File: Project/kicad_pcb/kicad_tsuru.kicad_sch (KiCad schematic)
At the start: 71 parts, among them J1 USB_C_Receptacle_USB2.0, J2 Conn_ARM_SWD_TagConnect_TC203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, J3 Conn_01x05_Pin, SW1 RotaryEncoder_Switch, U2 AP2112K-3.3, U3 STM32F072C8Tx

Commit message: cap & HS collision fixed
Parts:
- SW?: footprint PCM_marbastlib-various:SW_SPST_SKQG_WithStem -> Button_Switch_SMD:SW_Push_SPST_NO_Alps_SKRK
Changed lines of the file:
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@@
       (effects (font (size 1.27 1.27)))
     )
-    (property "Footprint" "PCM_marbastlib-various:SW_SPST_SKQG_WithStem" (at 245.11 139.065 0)
+    (property "Footprint" "Button_Switch_SMD:SW_Push_SPST_NO_Alps_SKRK" (at 245.11 139.065 0)
       (effects (font (size 1.27 1.27)) hide)
     )

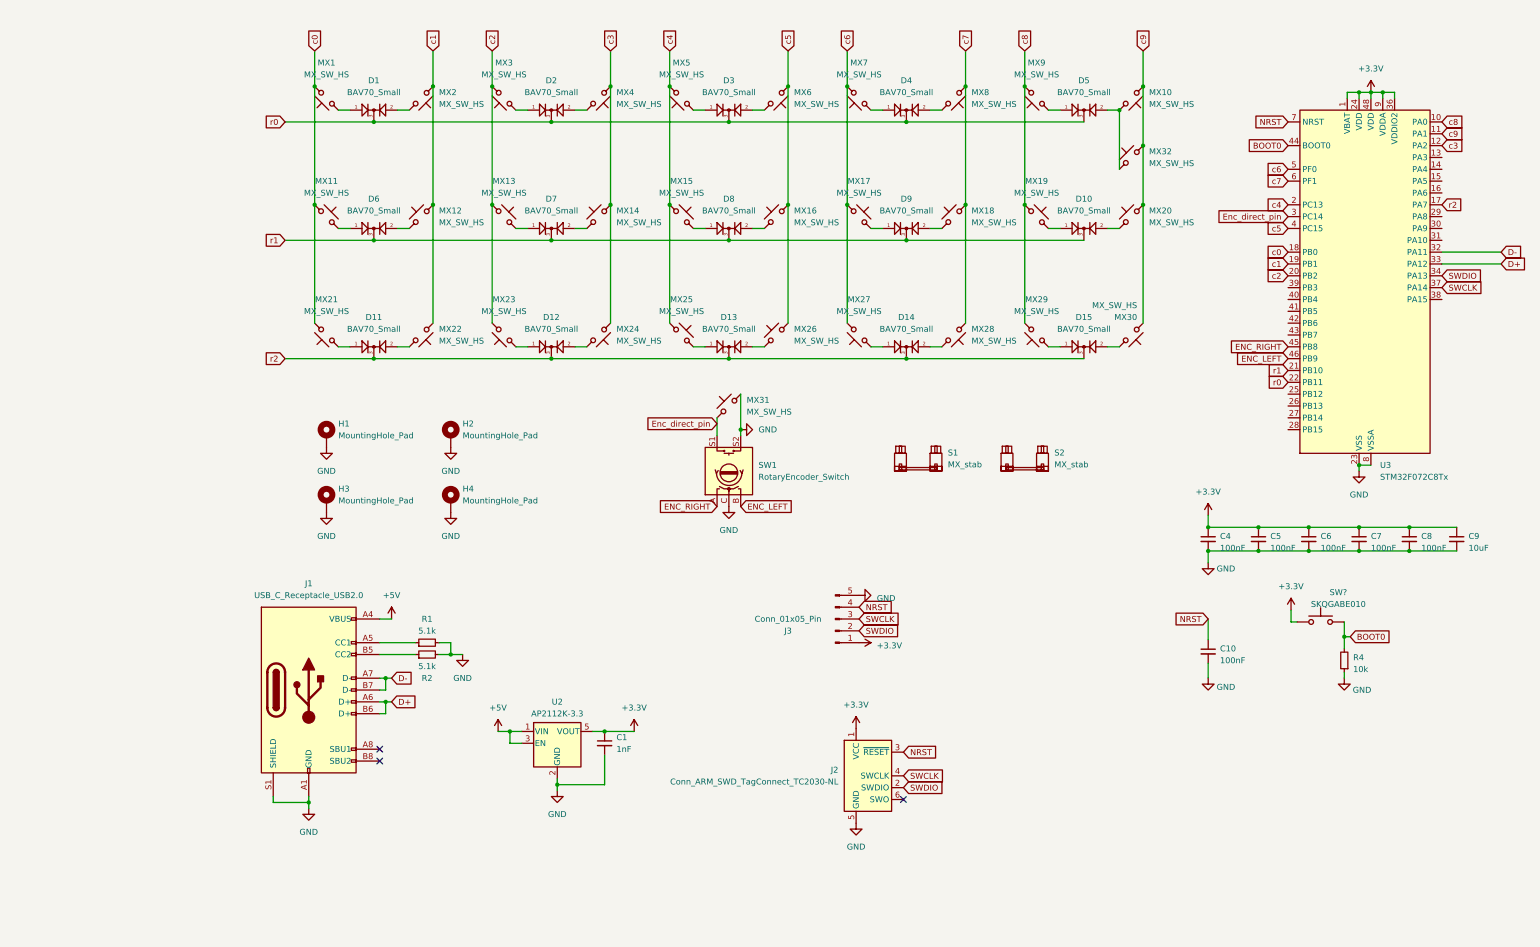
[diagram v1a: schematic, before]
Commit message: optional underglow added, fuze & esd protection added
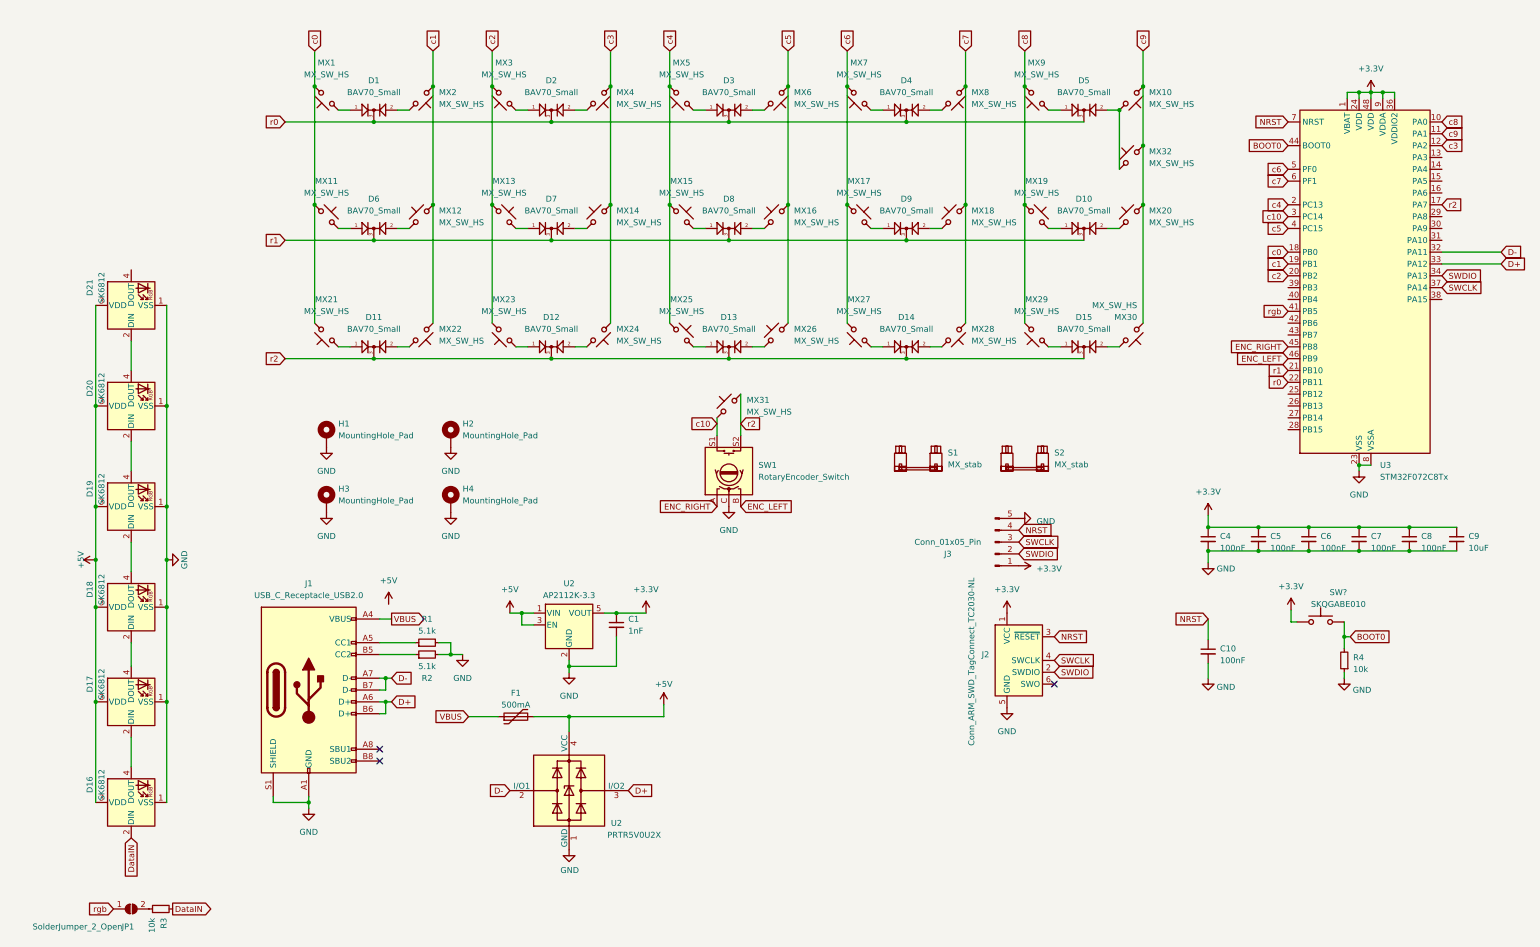
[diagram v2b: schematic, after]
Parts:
- added D16, D17, D18, D19, D20, D21: SK6812, LED_SMD:LED_SK6812_PLCC4_5.0x5.0mm_P3.2mm, symbol LED:SK6812
- added F1: 500mA, Fuse:Fuse_1206_3216Metric_Pad1.42x1.75mm_HandSolder, symbol Device:Polyfuse
- added JP1: SolderJumper_2_Open, Jumper:SolderJumper-2_P1.3mm_Open_RoundedPad1.0x1.5mm, symbol Jumper:SolderJumper_2_Open
- added R3: 10k, Resistor_SMD:R_0805_2012Metric_Pad1.20x1.40mm_HandSolder, symbol Device:R_Small
- added U2: PRTR5V0U2X, Package_TO_SOT_SMD:SOT-143_Handsoldering, symbol Power_Protection:PRTR5V0U2X
- U2: footprint Package_TO_SOT_SMD:SOT-23-5 -> Package_TO_SOT_SMD:SOT-23-5_HandSoldering
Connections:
- net +5V: now also D16.3 (VDD), D17.3 (VDD), D18.3 (VDD), D19.3 (VDD), D20.3 (VDD), D21.3 (VDD), F1.2, U2.4 (VCC); no longer J1.A4 (VBUS), J1.A9 (VBUS), J1.B4 (VBUS), J1.B9 (VBUS)
- net D+: now also U2.3 (I/O2)
- net D-: now also U2.2 (I/O1)
- net GND: now also D16.1 (VSS), D17.1 (VSS), D18.1 (VSS), D19.1 (VSS), D20.1 (VSS), D21.1 (VSS), U2.1 (GND); no longer MX31.2, SW1.S2
- net r2: now also MX31.2, SW1.S2
- net rgb: now reaches U3.41 (PB5)
- net rgb: now also JP1.1 (A)
- net Enc_direct_pin renamed c10
- new net: D20.4 (DOUT), D21.2 (DIN)
- new net: JP1.2 (B), R3.1
- new net: D16.4 (DOUT), D17.2 (DIN)
- new net: D17.4 (DOUT), D18.2 (DIN)
- new net: D18.4 (DOUT), D19.2 (DIN)
- new net: D19.4 (DOUT), D20.2 (DIN)
- new net DataIN: D16.2 (DIN), R3.2
- new net VBUS: F1.1, J1.A4 (VBUS), J1.A9 (VBUS), J1.B4 (VBUS), J1.B9 (VBUS)
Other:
- moved on the sheet: C1, J2, J3, U2

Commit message: readme update
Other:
- moved on the sheet: C1, C10, C4, C5, C6, C7, C8, C9, D16, D17, D18, D19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
